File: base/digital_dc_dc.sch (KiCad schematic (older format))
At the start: 34 parts, among them U14 AMS1117-5.0, U15 AMS1117-5.0, U17 LM2596S-ADJ

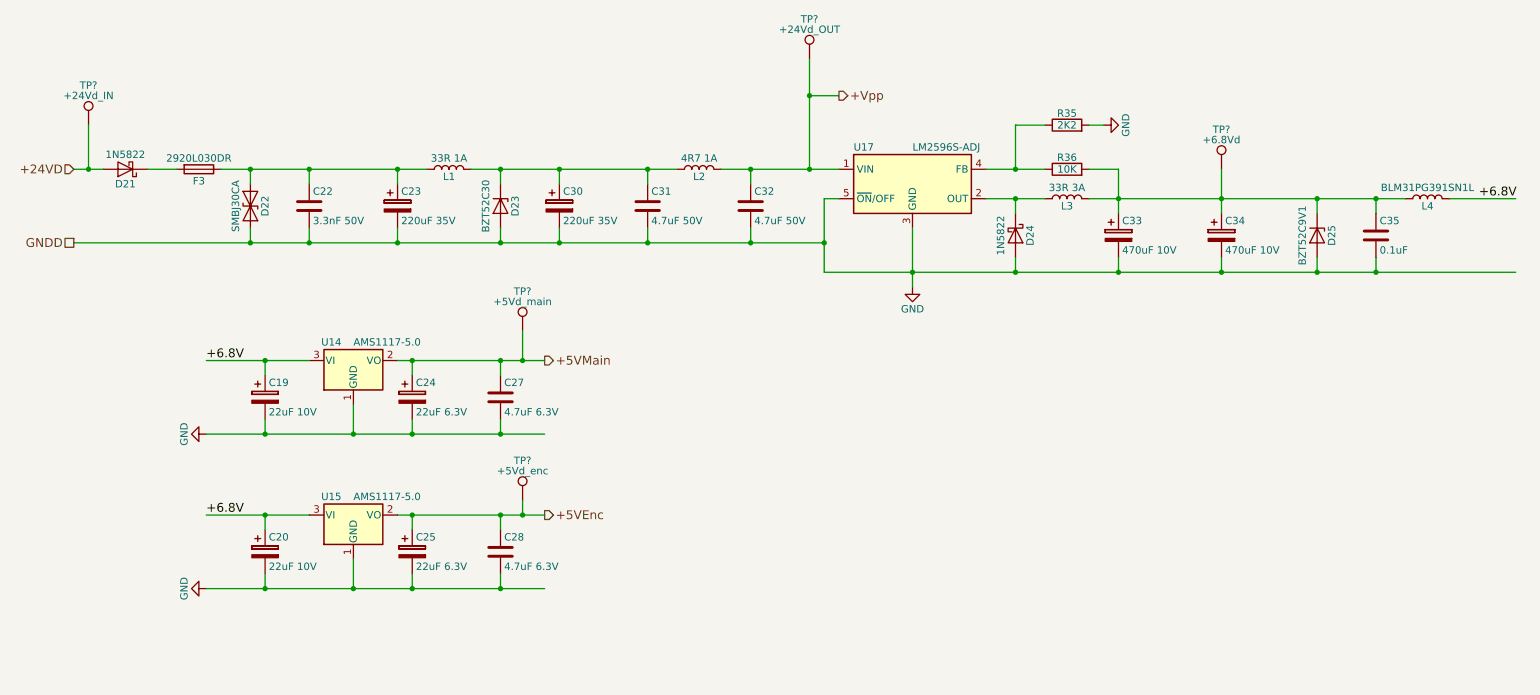
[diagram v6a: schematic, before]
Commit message: annotate sch
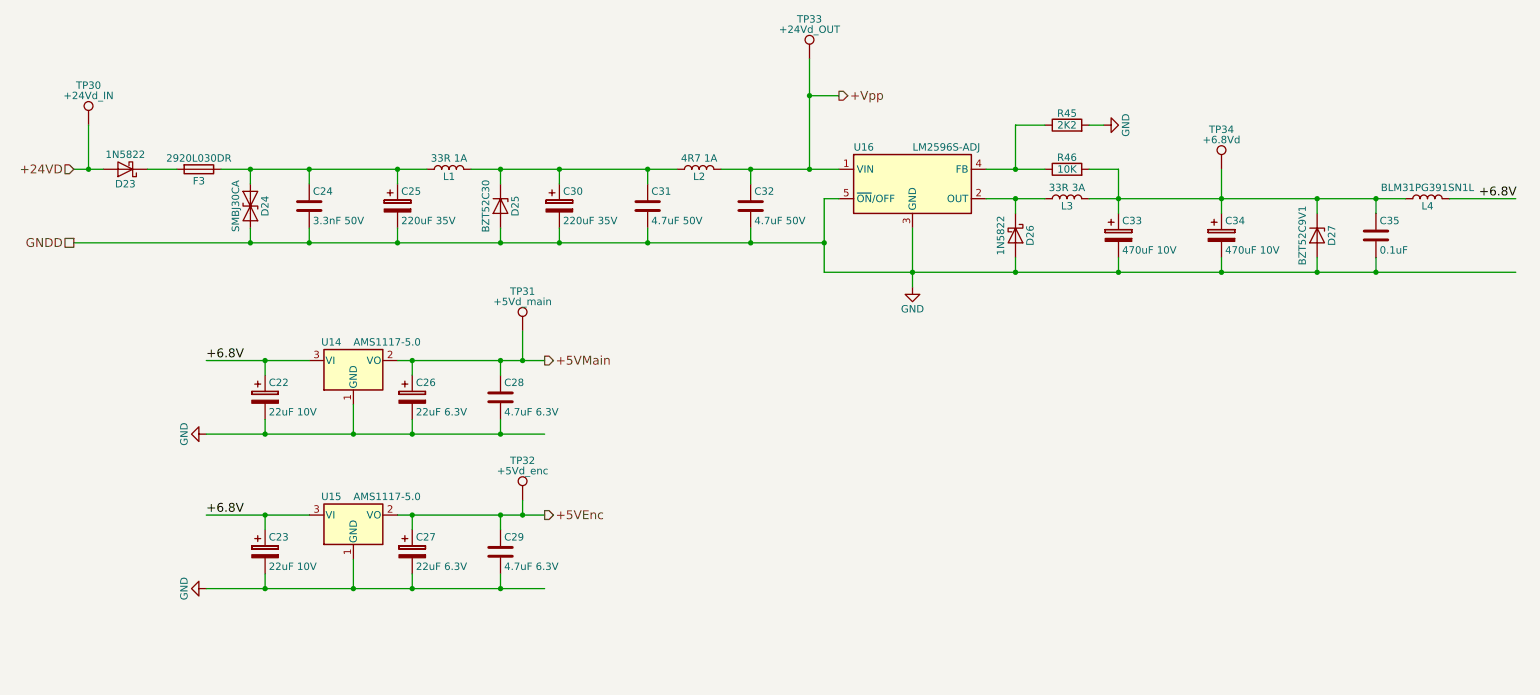
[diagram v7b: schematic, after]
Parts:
- gave numbers to parts that had none: 5
- renumbered C19 to C22, C20 to C23, C22 to C24, C23 to C25, C24 to C26, C25 to C27, C27 to C28, C28 to C29, D21 to D23, D22 to D24, D23 to D25, D24 to D26, D25 to D27, R35 to R45, R36 to R46, U17 to U16
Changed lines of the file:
@@
 GNDD
 $Comp
-L 1N5822 D21
+L 1N5822 D23
 U 1 1 5A392E0A
 P 1550 3000
-F 0 "D21" H 1550 3100 50  0000 C CNN
+F 0 "D23" H 1550 3100 50  0000 C CNN
 F 1 "1N5822" H 1550 2900 50  0000 C CNN
 F 2 "Diode_SMD:D_SMA" H 1550 2825 50  0001 C CNN
@@
 $EndComp
 $Comp
-L D_TVS D22
+L D_TVS D24
 U 1 1 5A3934E7
 P 2400 3250
-F 0 "D22" H 2400 3350 50  0000 C CNN
+F 0 "D24" H 2400 3350 50  0000 C CNN
 F 1 "SMBJ30CA" H 2400 3150 50  0000 C CNN
 F 2 "Diode_SMD:D_SMB" H 2400 3250 50  0001 C CNN
@@
 $EndComp
 $Comp
-L C C22
+L C C24
 U 1 1 5A393804
 P 2800 3250
-F 0 "C22" H 2825 3350 50  0000 L CNN
+F 0 "C24" H 2825 3350 50  0000 L CNN
 F 1 "3.3nF 50V" H 2825 3150 50  0000 L CNN
 F 2 "Capacitor_SMD:C_0603_1608Metric" H 2838 3100 50  0001 C CNN
@@
 $EndComp
 $Comp
-L CP C23
+L CP C25
 U 1 1 5A393B3D
 P 3400 3250
-F 0 "C23" H 3425 3350 50  0000 L CNN
+F 0 "C25" H 3425 3350 50  0000 L CNN
 F 1 "220uF 35V" H 3425 3150 50  0000 L CNN
 F 2 "Capacitor_SMD:CP_Elec_8x10" H 3438 3100 50  0001 C CNN
@@
 $EndComp
 $Comp
-L D_Zener D23
+L D_Zener D25
 U 1 1 5A394214
 P 4100 3250
-F 0 "D23" H 4100 3350 50  0000 C CNN
+F 0 "D25" H 4100 3350 50  0000 C CNN
 F 1 "BZT52C30" H 4100 3150 50  0000 C CNN
 F 2 "Diode_SMD:D_SOD-123" H 4100 3250 50  0001 C CNN
@@
 $EndComp
 $Comp
-L LM2596S-ADJ U17
+L LM2596S-ADJ U16
 U 1 1 5A395D36
 P 6900 3100
-F 0 "U17" H 6500 3350 50  0000 L CNN
+F 0 "U16" H 6500 3350 50  0000 L CNN
 F 1 "LM2596S-ADJ" H 6900 3350 50  0000 L CNN
 F 2 "Package_TO_SOT_SMD:TO-263-5_TabPin3" H 6950 2850 50  0001 L CIN
@@
 $EndComp
 $Comp
-L 1N5822 D24
+L 1N5822 D26
 U 1 1 5A395F02
 P 7600 3450
-F 0 "D24" H 7600 3550 50  0000 C CNN
+F 0 "D26" H 7600 3550 50  0000 C CNN
 F 1 "1N5822" H 7600 3350 50  0000 C CNN
 F 2 "Diode_SMD:D_SMA" H 7600 3275 50  0001 C CNN
@@
 $EndComp
 $Comp
-L R R36
+L R R46
 U 1 1 5A396200
 P 7950 3000
-F 0 "R36" V 8030 3000 50  0000 C CNN
+F 0 "R46" V 8030 3000 50  0000 C CNN
 F 1 "10K" V 7950 3000 50  0000 C CNN
 F 2 "Resistor_SMD:R_0603_1608Metric" V 7880 3000 50  0001 C CNN
@@
 $EndComp
 $Comp
-L R R35
+L R R45
 U 1 1 5A396375
 P 7950 2700
-F 0 "R35" V 8030 2700 50  0000 C CNN
+F 0 "R45" V 8030 2700 50  0000 C CNN
 F 1 "2K2" V 7950 2700 50  0000 C CNN
 F 2 "Resistor_SMD:R_0603_1608Metric" V 7880 2700 50  0001 C CNN
@@
 $EndComp
 $Comp
-L GND #PWR020
+L GND #PWR29
 U 1 1 5A3963F4
 P 6900 3800
-F 0 "#PWR020" H 6900 3550 50  0001 C CNN
+F 0 "#PWR29" H 6900 3550 50  0001 C CNN
 F 1 "GND" H 6900 3650 50  0000 C CNN
 F 2 "" H 6900 3800 50  0001 C CNN
@@
 $EndComp
 $Comp
-L GND #PWR021
+L GND #PWR30
 U 1 1 5A3964B9
 P 8200 2700
-F 0 "#PWR021" H 8200 2450 50  0001 C CNN
+F 0 "#PWR30" H 8200 2450 50  0001 C CNN
 F 1 "GND" H 8200 2550 50  0000 C CNN
 F 2 "" H 8200 2700 50  0001 C CNN
@@
 $EndComp
 $Comp
-L D_Zener D25
+L D_Zener D27
 U 1 1 5A396751
 P 9650 3450
-F 0 "D25" H 9650 3550 50  0000 C CNN
+F 0 "D27" H 9650 3550 50  0000 C CNN
 F 1 "BZT52C9V1" H 9650 3350 50  0000 C CNN
 F 2 "Diode_SMD:D_SOD-123" H 9650 3450 50  0001 C CNN
@@
 +6.8V
 $Comp
-L CP C19
+L CP C22
 U 1 1 5A3971EB
 P 2500 4550
-F 0 "C19" H 2525 4650 50  0000 L CNN
+F 0 "C22" H 2525 4650 50  0000 L CNN
 F 1 "22uF 10V" H 2525 4450 50  0000 L CNN
 F 2 "Capacitor_Tantalum_SMD:CP_EIA-3216-18_Kemet-A" H 2538 4400 50  0001 C CNN
@@
 +6.8V
 $Comp
-L GND #PWR022
+L GND #PWR27
 U 1 1 5A3987CE
 P 2100 4800
-F 0 "#PWR022" H 2100 4550 50  0001 C CNN
+F 0 "#PWR27" H 2100 4550 50  0001 C CNN
 F 1 "GND" H 2100 4650 50  0000 C CNN
 F 2 "" H 2100 4800 50  0001 C CNN
@@
 $EndComp
 $Comp
-L CP C24
+L CP C26
 U 1 1 5A3988D5
 P 3500 4550
-F 0 "C24" H 3525 4650 50  0000 L CNN
+F 0 "C26" H 3525 4650 50  0000 L CNN
 F 1 "22uF 6.3V" H 3525 4450 50  0000 L CNN
 F 2 "Capacitor_Tantalum_SMD:CP_EIA-3216-18_Kemet-A" H 3538 4400 50  0001 C CNN
@@
 $EndComp
 $Comp
-L C C27
+L C C28
 U 1 1 5A398AEE
 P 4100 4550
-F 0 "C27" H 4125 4650 50  0000 L CNN
+F 0 "C28" H 4125 4650 50  0000 L CNN
 F 1 "4.7uF 6.3V" H 4125 4450 50  0000 L CNN
 F 2 "Capacitor_SMD:C_0603_1608Metric" H 4138 4400 50  0001 C CNN
@@
 $EndComp
 $Comp
-L CP C20
+L CP C23
 U 1 1 5A398DF8
 P 2500 5600
-F 0 "C20" H 2525 5700 50  0000 L CNN
+F 0 "C23" H 2525 5700 50  0000 L CNN
 F 1 "22uF 10V" H 2525 5500 50  0000 L CNN
 F 2 "Capacitor_Tantalum_SMD:CP_EIA-3216-18_Kemet-A" H 2538 5450 50  0001 C CNN
@@
 +6.8V
 $Comp
-L GND #PWR023
+L GND #PWR28
 U 1 1 5A398E0C
 P 2100 5850
-F 0 "#PWR023" H 2100 5600 50  0001 C CNN
+F 0 "#PWR28" H 2100 5600 50  0001 C CNN
 F 1 "GND" H 2100 5700 50  0000 C CNN
 F 2 "" H 2100 5850 50  0001 C CNN
@@
 $EndComp
 $Comp
-L CP C25
+L CP C27
 U 1 1 5A398E13
 P 3500 5600
-F 0 "C25" H 3525 5700 50  0000 L CNN
+F 0 "C27" H 3525 5700 50  0000 L CNN
 F 1 "22uF 6.3V" H 3525 5500 50  0000 L CNN
 F 2 "Capacitor_Tantalum_SMD:CP_EIA-3216-18_Kemet-A" H 3538 5450 50  0001 C CNN
@@
 $EndComp
 $Comp
-L C C28
+L C C29
 U 1 1 5A398E1E
 P 4100 5600
-F 0 "C28" H 4125 5700 50  0000 L CNN
+F 0 "C29" H 4125 5700 50  0000 L CNN
 F 1 "4.7uF 6.3V" H 4125 5500 50  0000 L CNN
 F 2 "Capacitor_SMD:C_0603_1608Metric" H 4138 5450 50  0001 C CNN
@@
 Connection ~ 6200 3000
 $Comp
-L Test_Point TP?
+L Test_Point TP31
 U 1 1 5A49ED26
 P 4250 4100
-F 0 "TP?" H 4250 4370 50  0000 C CNN
+F 0 "TP31" H 4250 4370 50  0000 C CNN
 F 1 "+5Vd_main" H 4250 4300 50  0000 C CNN
 F 2 "" H 4450 4100 50  0001 C CNN
@@
 Connection ~ 4250 4300
 $Comp
-L Test_Point TP?
+L Test_Point TP32
 U 1 1 5A49EF64
 P 4250 5250
-F 0 "TP?" H 4250 5520 50  0000 C CNN
+F 0 "TP32" H 4250 5520 50  0000 C CNN
 F 1 "+5Vd_enc" H 4250 5450 50  0000 C CNN
 F 2 "" H 4450 5250 50  0001 C CNN
@@
 Connection ~ 4250 5350
 $Comp
-L Test_Point TP?
+L Test_Point TP30
 U 1 1 5A4A0D23
 P 1300 2700
-F 0 "TP?" H 1300 2970 50  0000 C CNN
+F 0 "TP30" H 1300 2970 50  0000 C CNN
 F 1 "+24Vd_IN" H 1300 2900 50  0000 C CNN
 F 2 "" H 1500 2700 50  0001 C CNN
@@
 Connection ~ 1300 3000
 $Comp
-L Test_Point TP?
+L Test_Point TP33
 U 1 1 5A4A0FEB
 P 6200 2250
-F 0 "TP?" H 6200 2520 50  0000 C CNN
+F 0 "TP33" H 6200 2520 50  0000 C CNN
 F 1 "+24Vd_OUT" H 6200 2450 50  0000 C CNN
 F 2 "" H 6400 2250 50  0001 C CNN
@@
 Connection ~ 6200 2500
 $Comp
-L Test_Point TP?
+L Test_Point TP34
 U 1 1 5A456659
 P 9000 3000
-F 0 "TP?" H 9000 3270 50  0000 C CNN
+F 0 "TP34" H 9000 3270 50  0000 C CNN
 F 1 "+6.8Vd" H 9000 3200 50  0000 C CNN
 F 2 "" H 9200 3000 50  0001 C CNN

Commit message: added footprints, created netlist
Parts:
- TP30, TP31, TP32, TP33, TP34: footprint (none) -> TestPoint:TestPoint_Pad_D1.5mm
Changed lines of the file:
@@
 $EndComp
 $Comp
-L GND #PWR29
+L GND #PWR027
 U 1 1 5A3963F4
 P 6900 3800
-F 0 "#PWR29" H 6900 3550 50  0001 C CNN
+F 0 "#PWR027" H 6900 3550 50  0001 C CNN
 F 1 "GND" H 6900 3650 50  0000 C CNN
 F 2 "" H 6900 3800 50  0001 C CNN
@@
 $EndComp
 $Comp
-L GND #PWR30
+L GND #PWR028
 U 1 1 5A3964B9
 P 8200 2700
-F 0 "#PWR30" H 8200 2450 50  0001 C CNN
+F 0 "#PWR028" H 8200 2450 50  0001 C CNN
 F 1 "GND" H 8200 2550 50  0000 C CNN
 F 2 "" H 8200 2700 50  0001 C CNN
@@
 +6.8V
 $Comp
-L GND #PWR27
+L GND #PWR029
 U 1 1 5A3987CE
 P 2100 4800
-F 0 "#PWR27" H 2100 4550 50  0001 C CNN
+F 0 "#PWR029" H 2100 4550 50  0001 C CNN
 F 1 "GND" H 2100 4650 50  0000 C CNN
 F 2 "" H 2100 4800 50  0001 C CNN
@@
 +6.8V
 $Comp
-L GND #PWR28
+L GND #PWR030
 U 1 1 5A398E0C
 P 2100 5850
-F 0 "#PWR28" H 2100 5600 50  0001 C CNN
+F 0 "#PWR030" H 2100 5600 50  0001 C CNN
 F 1 "GND" H 2100 5700 50  0000 C CNN
 F 2 "" H 2100 5850 50  0001 C CNN
@@
 F 0 "TP31" H 4250 4370 50  0000 C CNN
 F 1 "+5Vd_main" H 4250 4300 50  0000 C CNN
-F 2 "" H 4450 4100 50  0001 C CNN
+F 2 "TestPoint:TestPoint_Pad_D1.5mm" H 4450 4100 50  0001 C CNN
 F 3 "" H 4450 4100 50  0001 C CNN
 	1    4250 4100
@@
 F 0 "TP32" H 4250 5520 50  0000 C CNN
 F 1 "+5Vd_enc" H 4250 5450 50  0000 C CNN
-F 2 "" H 4450 5250 50  0001 C CNN
+F 2 "TestPoint:TestPoint_Pad_D1.5mm" H 4450 5250 50  0001 C CNN
 F 3 "" H 4450 5250 50  0001 C CNN
 	1    4250 5250
@@
 F 0 "TP30" H 1300 2970 50  0000 C CNN
 F 1 "+24Vd_IN" H 1300 2900 50  0000 C CNN
-F 2 "" H 1500 2700 50  0001 C CNN
+F 2 "TestPoint:TestPoint_Pad_D1.5mm" H 1500 2700 50  0001 C CNN
 F 3 "" H 1500 2700 50  0001 C CNN
 	1    1300 2700
@@
 F 0 "TP33" H 6200 2520 50  0000 C CNN
 F 1 "+24Vd_OUT" H 6200 2450 50  0000 C CNN
-F 2 "" H 6400 2250 50  0001 C CNN
+F 2 "TestPoint:TestPoint_Pad_D1.5mm" H 6400 2250 50  0001 C CNN
 F 3 "" H 6400 2250 50  0001 C CNN
 	1    6200 2250
@@
 F 0 "TP34" H 9000 3270 50  0000 C CNN
 F 1 "+6.8Vd" H 9000 3200 50  0000 C CNN
-F 2 "" H 9200 3000 50  0001 C CNN
+F 2 "TestPoint:TestPoint_Pad_D1.5mm" H 9200 3000 50  0001 C CNN
 F 3 "" H 9200 3000 50  0001 C CNN
 	1    9000 3000
